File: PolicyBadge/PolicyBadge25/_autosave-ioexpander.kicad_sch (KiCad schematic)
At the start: 25 parts, among them Q1 2N7002, U10 YX-SMD5020, U9 TCA9555PWR

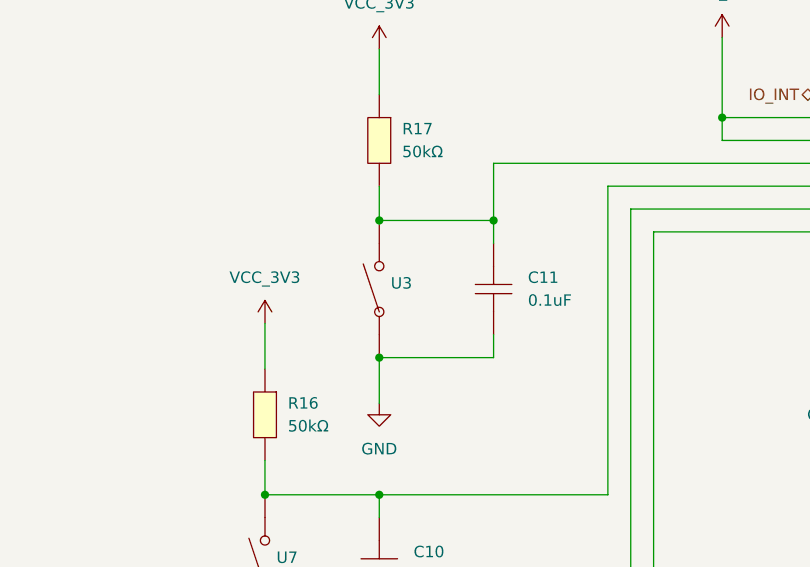
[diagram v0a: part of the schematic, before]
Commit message: minor updates
imported new switch footprint and schematic symbol. sync'ed the PCB to add R23, R5, R6. annotated.
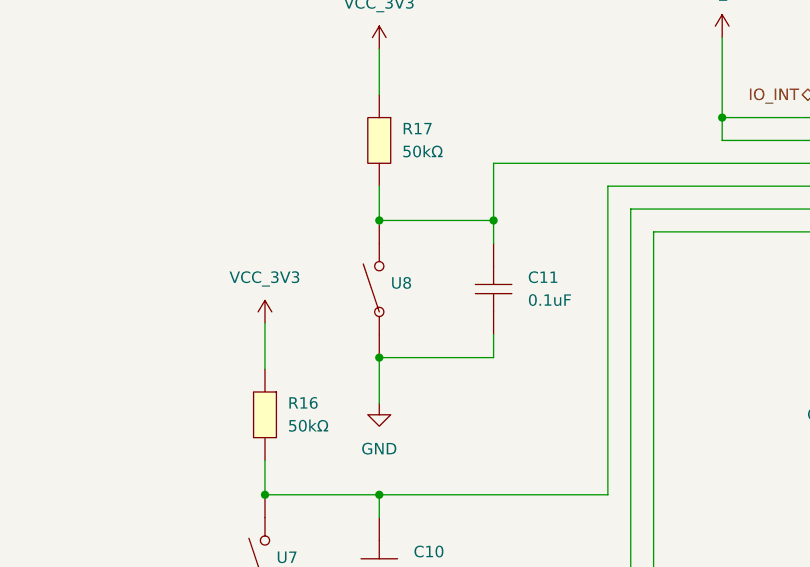
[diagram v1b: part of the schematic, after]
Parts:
- renumbered U3 to U8
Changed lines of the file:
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@@
 		(dnp no)
 		(fields_autoplaced yes)
-		(property "Reference" "U3"
+		(property "Reference" "U8"
 			(at 97.79 71.7549 90)
 			(effects
@@
 			(project "PolicyBadge25"
 				(path "/3911717a-8f19-42c2-8f04-ebfae4e12db6/0606a99a-a678-47a5-968e-d91d30829907"
-					(reference "U3")
+					(reference "U8")
 					(unit 1)
 				)
